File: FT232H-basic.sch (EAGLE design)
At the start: 27 parts, among them IC1 FT232H

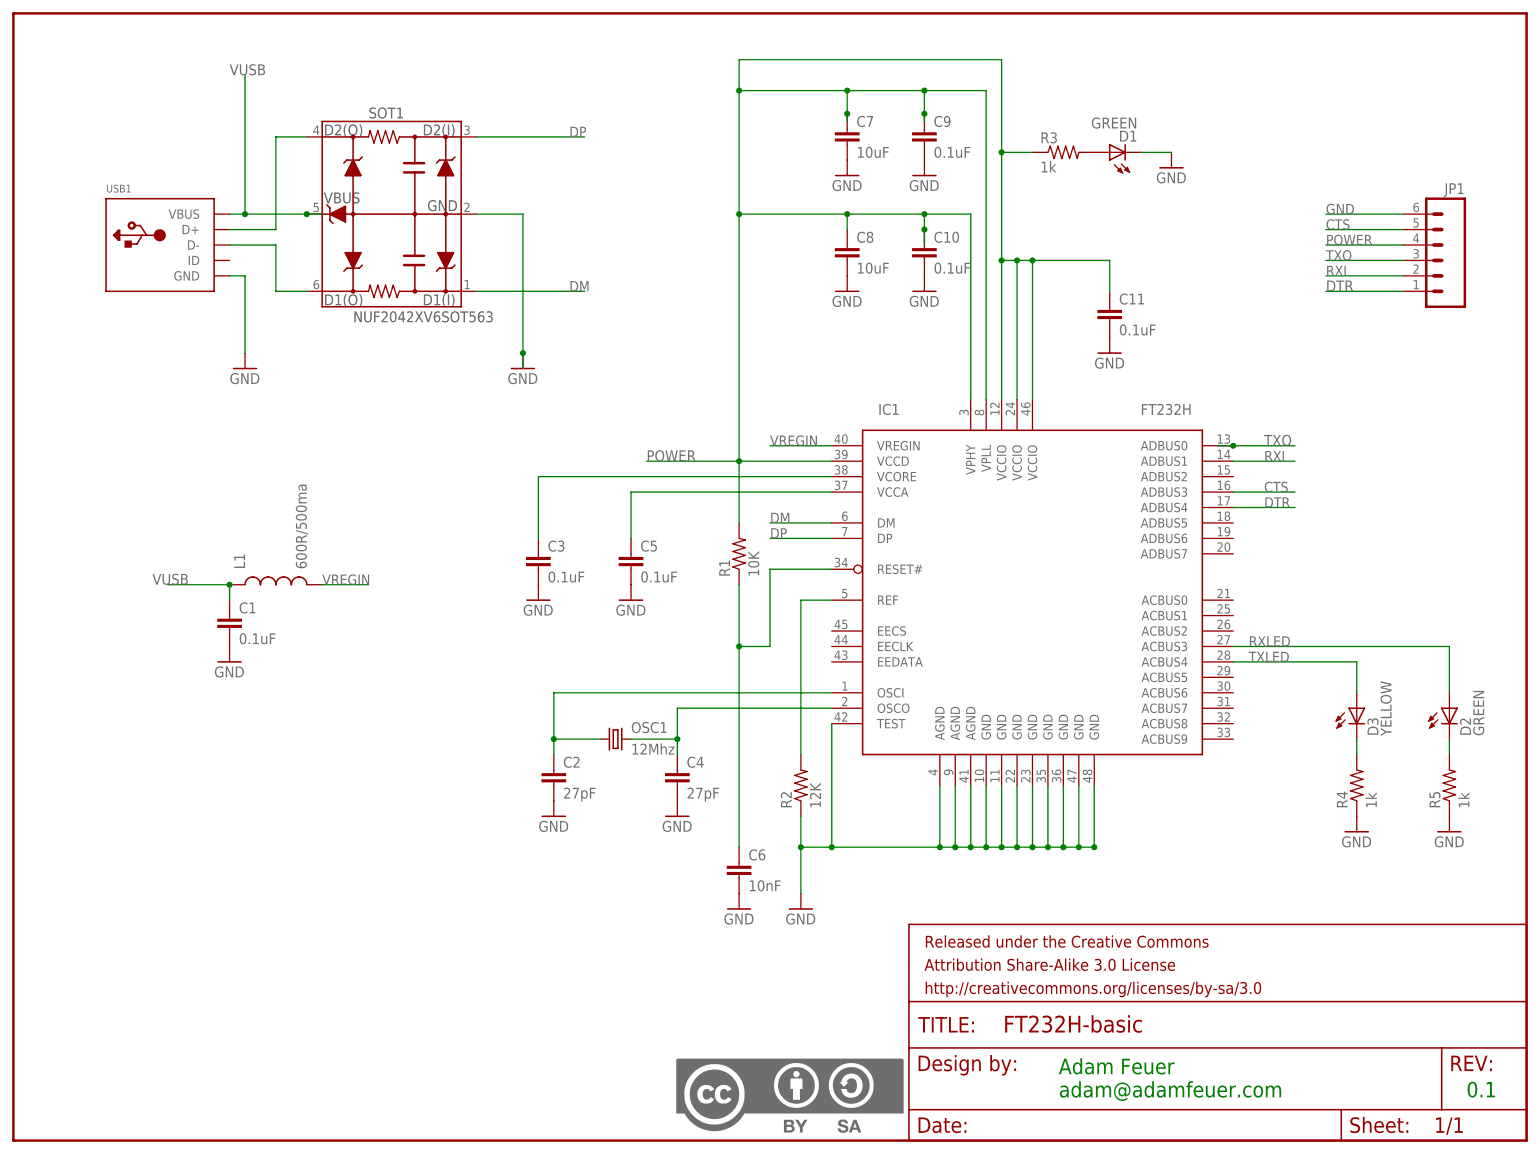
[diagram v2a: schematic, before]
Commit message: minor changes - removed CC logo from schematic (still on board); made layers visible
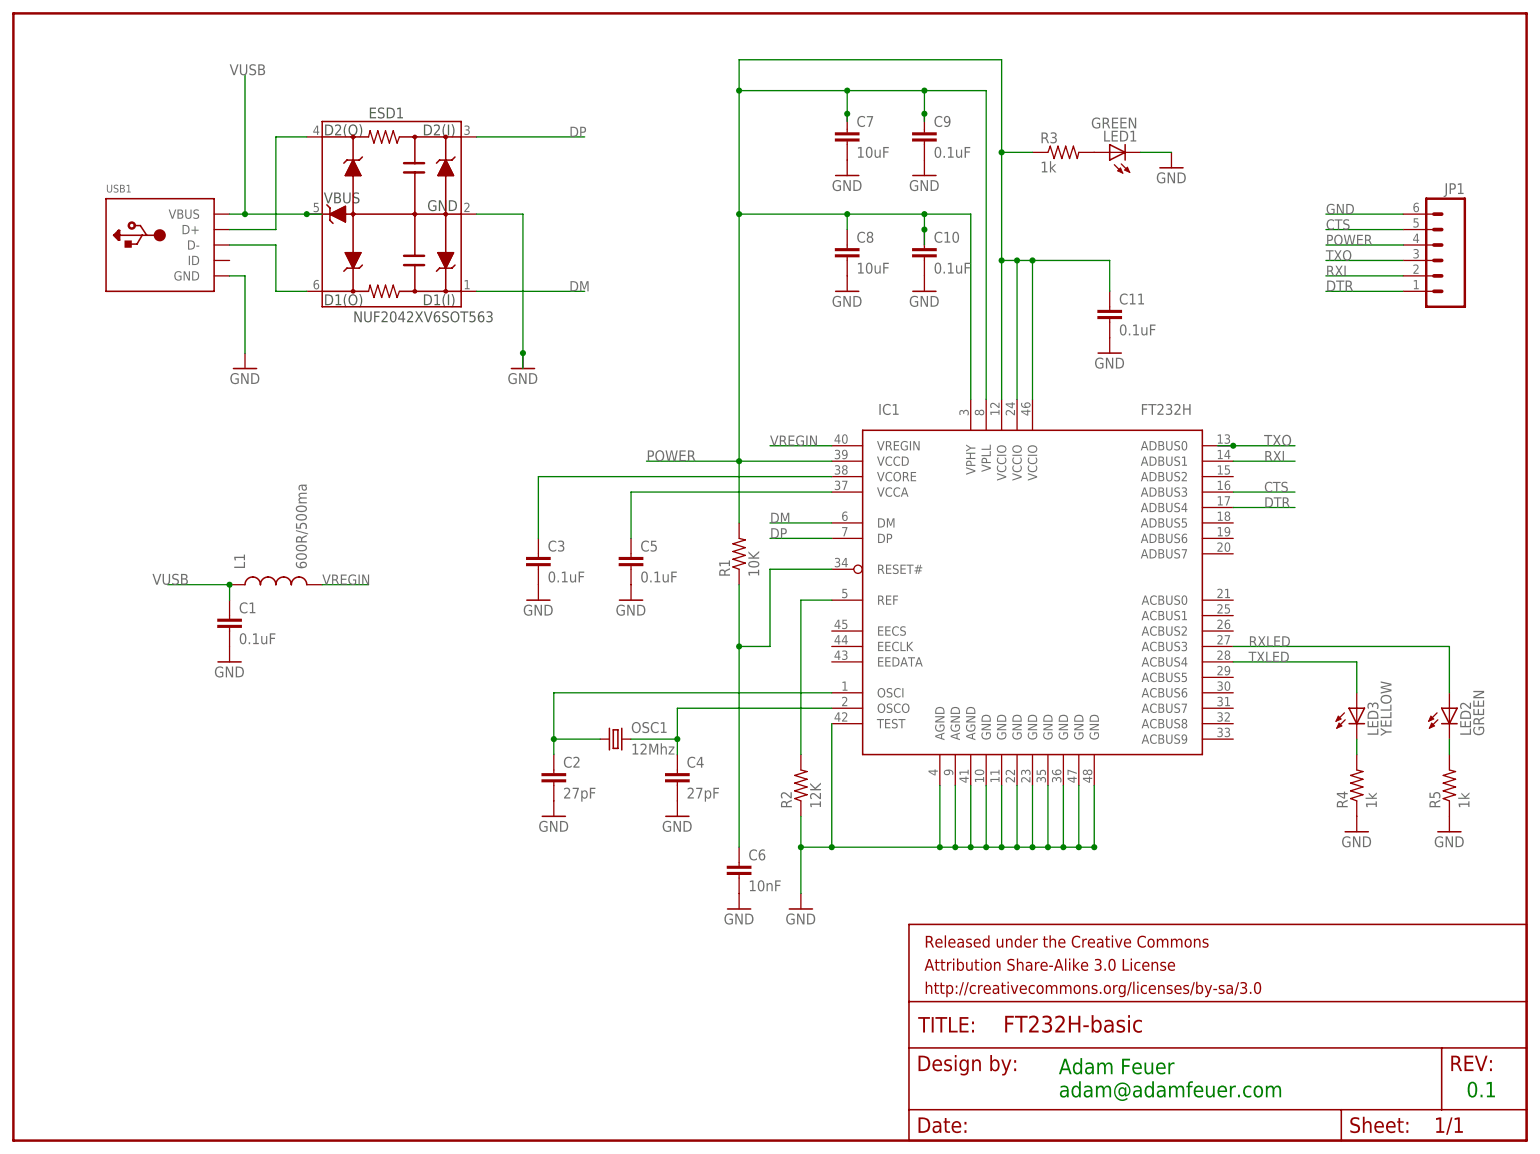
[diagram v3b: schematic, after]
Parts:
- removed U$2: CC-BY-SA, creative-commons:CC-BY-SA
- renumbered D1 to LED1, D2 to LED2, D3 to LED3, SOT1 to ESD1
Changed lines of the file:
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@@
 <part name="GND13" library="SparkFun-Aesthetics" deviceset="GND" device=""/>
 <part name="L1" library="SparkFun-Passives" deviceset="INDUCTOR" device="0603" value="600R/500ma"/>
-<part name="SOT1" library="USB-ESD-protection" deviceset="NUF2042XV6" device="SOT563"/>
+<part name="ESD1" library="USB-ESD-protection" deviceset="NUF2042XV6" device="SOT563"/>
 <part name="USB1" library="USB-Mini-Molex" deviceset="USB-MINIB" device="TH-SLOT"/>
 <part name="GND14" library="SparkFun-Aesthetics" deviceset="GND" device=""/>
 <part name="GND15" library="SparkFun-Aesthetics" deviceset="GND" device=""/>
 <part name="JP1" library="SparkFun-Connectors" deviceset="M06" device="SMD-FEMALE-V2"/>
-<part name="D2" library="SparkFun-LED" deviceset="LED-GREEN" device="0603" value="GREEN"/>
-<part name="D3" library="SparkFun-LED" deviceset="LED-YELLOW" device="0603" value="YELLOW"/>
+<part name="LED2" library="SparkFun-LED" deviceset="LED-GREEN" device="0603" value="GREEN"/>
+<part name="LED3" library="SparkFun-LED" deviceset="LED-YELLOW" device="0603" value="YELLOW"/>
 <part name="R4" library="SparkFun-Resistors" deviceset="1K-1%" device="" value="1k"/>
 <part name="R5" library="SparkFun-Resistors" deviceset="1K-1%" device="" value="1k"/>
 <part name="GND16" library="SparkFun-Aesthetics" deviceset="GND" device=""/>
 <part name="GND17" library="SparkFun-Aesthetics" deviceset="GND" device=""/>
-<part name="D1" library="SparkFun-LED" deviceset="LED-GREEN" device="0603" value="GREEN"/>
+<part name="LED1" library="SparkFun-LED" deviceset="LED-GREEN" device="0603" value="GREEN"/>
 <part name="OSC1" library="SparkFun-FreqCtrl" deviceset="CRYSTAL" device="5X3" value="12Mhz"/>
 <part name="FRAME1" library="SparkFun-Aesthetics" deviceset="FRAME-LETTER" device=""/>
-<part name="U$2" library="creative-commons" deviceset="CC-BY-SA" device=""/>
 </parts>
 <sheets>
@@
 <instance part="GND13" gate="1" x="35.56" y="78.74"/>
 <instance part="L1" gate="G$1" x="43.18" y="91.44" rot="R90"/>
-<instance part="SOT1" gate="G$1" x="63.5" y="152.4"/>
+<instance part="ESD1" gate="G$1" x="63.5" y="152.4"/>
 <instance part="USB1" gate="G$1" x="25.4" y="147.32"/>
 <instance part="GND14" gate="1" x="38.1" y="127"/>
 <instance part="GND15" gate="1" x="83.82" y="127"/>
 <instance part="JP1" gate="G$1" x="233.68" y="144.78" rot="MR0"/>
-<instance part="D2" gate="G$1" x="236.22" y="71.12"/>
-<instance part="D3" gate="G$1" x="220.98" y="71.12"/>
+<instance part="LED2" gate="G$1" x="236.22" y="71.12"/>
+<instance part="LED3" gate="G$1" x="220.98" y="71.12"/>
 <instance part="R4" gate="G$1" x="220.98" y="58.42" rot="R90"/>
 <instance part="R5" gate="G$1" x="236.22" y="58.42" rot="R90"/>
 <instance part="GND16" gate="1" x="220.98" y="50.8"/>
 <instance part="GND17" gate="1" x="236.22" y="50.8"/>
-<instance part="D1" gate="G$1" x="180.34" y="162.56" rot="R90"/>
+<instance part="LED1" gate="G$1" x="180.34" y="162.56" rot="R90"/>
 <instance part="OSC1" gate="G$1" x="99.06" y="66.04"/>
 <instance part="FRAME1" gate="G$1" x="0" y="0"/>
 <instance part="FRAME1" gate="G$2" x="147.32" y="0"/>
-<instance part="U$2" gate="G$1" x="108.712" y="0.508"/>
 </instances>
 <busses>
@@
 <pinref part="GND12" gate="1" pin="GND"/>
 <wire x1="185.42" y1="162.56" x2="190.5" y2="162.56" width="0.1524" layer="91"/>
-<pinref part="D1" gate="G$1" pin="C"/>
+<pinref part="LED1" gate="G$1" pin="C"/>
 </segment>
 <segment>
@@
 </segment>
 <segment>
-<pinref part="SOT1" gate="G$1" pin="GND"/>
+<pinref part="ESD1" gate="G$1" pin="GND"/>
 <wire x1="76.2" y1="152.4" x2="83.82" y2="152.4" width="0.1524" layer="91"/>
 <wire x1="83.82" y1="152.4" x2="83.82" y2="129.54" width="0.1524" layer="91"/>
@@
 <pinref part="USB1" gate="G$1" pin="VBUS"/>
 <wire x1="35.56" y1="152.4" x2="38.1" y2="152.4" width="0.1524" layer="91"/>
-<pinref part="SOT1" gate="G$1" pin="VBUS"/>
+<pinref part="ESD1" gate="G$1" pin="VBUS"/>
 <wire x1="38.1" y1="152.4" x2="48.26" y2="152.4" width="0.1524" layer="91"/>
 <wire x1="48.26" y1="152.4" x2="50.8" y2="152.4" width="0.1524" layer="91"/>
@@
 <wire x1="35.56" y1="149.86" x2="43.18" y2="149.86" width="0.1524" layer="91"/>
 <wire x1="43.18" y1="149.86" x2="43.18" y2="165.1" width="0.1524" layer="91"/>
-<pinref part="SOT1" gate="G$1" pin="D2(O)"/>
+<pinref part="ESD1" gate="G$1" pin="D2(O)"/>
 <wire x1="43.18" y1="165.1" x2="48.26" y2="165.1" width="0.1524" layer="91"/>
 </segment>
@@
 <wire x1="35.56" y1="147.32" x2="43.18" y2="147.32" width="0.1524" layer="91"/>
 <wire x1="43.18" y1="147.32" x2="43.18" y2="139.7" width="0.1524" layer="91"/>
-<pinref part="SOT1" gate="G$1" pin="D1(O)"/>
+<pinref part="ESD1" gate="G$1" pin="D1(O)"/>
 <wire x1="43.18" y1="139.7" x2="48.26" y2="139.7" width="0.1524" layer="91"/>
 </segment>
@@
 <net name="DP" class="0">
 <segment>
-<pinref part="SOT1" gate="G$1" pin="D2(I)"/>
+<pinref part="ESD1" gate="G$1" pin="D2(I)"/>
 <wire x1="76.2" y1="165.1" x2="93.98" y2="165.1" width="0.1524" layer="91"/>
 <label x="91.44" y="165.1" size="1.6764" layer="95"/>
@@
 <net name="DM" class="0">
 <segment>
-<pinref part="SOT1" gate="G$1" pin="D1(I)"/>
+<pinref part="ESD1" gate="G$1" pin="D1(I)"/>
 <wire x1="76.2" y1="139.7" x2="93.98" y2="139.7" width="0.1524" layer="91"/>
 <label x="91.44" y="139.7" size="1.6764" layer="95"/>
@@
 <pinref part="IC1" gate="G$1" pin="ACBUS3"/>
 <label x="203.2" y="81.28" size="1.6764" layer="95"/>
-<pinref part="D2" gate="G$1" pin="A"/>
+<pinref part="LED2" gate="G$1" pin="A"/>
 <wire x1="200.66" y1="81.28" x2="236.22" y2="81.28" width="0.1524" layer="91"/>
 <wire x1="236.22" y1="81.28" x2="236.22" y2="73.66" width="0.1524" layer="91"/>
@@
 <pinref part="IC1" gate="G$1" pin="ACBUS4"/>
 <label x="203.2" y="78.74" size="1.6764" layer="95"/>
-<pinref part="D3" gate="G$1" pin="A"/>
+<pinref part="LED3" gate="G$1" pin="A"/>
 <wire x1="200.66" y1="78.74" x2="220.98" y2="78.74" width="0.1524" layer="91"/>
 <wire x1="220.98" y1="78.74" x2="220.98" y2="73.66" width="0.1524" layer="91"/>
@@
 <net name="N$10" class="0">
 <segment>
-<pinref part="D3" gate="G$1" pin="C"/>
+<pinref part="LED3" gate="G$1" pin="C"/>
 <pinref part="R4" gate="G$1" pin="2"/>
 <wire x1="220.98" y1="66.04" x2="220.98" y2="63.5" width="0.1524" layer="91"/>
@@
 <net name="N$11" class="0">
 <segment>
-<pinref part="D2" gate="G$1" pin="C"/>
+<pinref part="LED2" gate="G$1" pin="C"/>
 <pinref part="R5" gate="G$1" pin="2"/>
 <wire x1="236.22" y1="66.04" x2="236.22" y2="63.5" width="0.1524" layer="91"/>
@@
 <segment>
 <pinref part="R3" gate="G$1" pin="2"/>
-<pinref part="D1" gate="G$1" pin="A"/>
-</segment>
-</net>
+<pinref part="LED1" gate="G$1" pin="A"/>
+</segment>
+</net>

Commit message: changed out ESD IC to USB 2.0 HS - NXP IP4220CZ6 ; added LittelFuse 0603; changed out connector to 1x06 female through hole
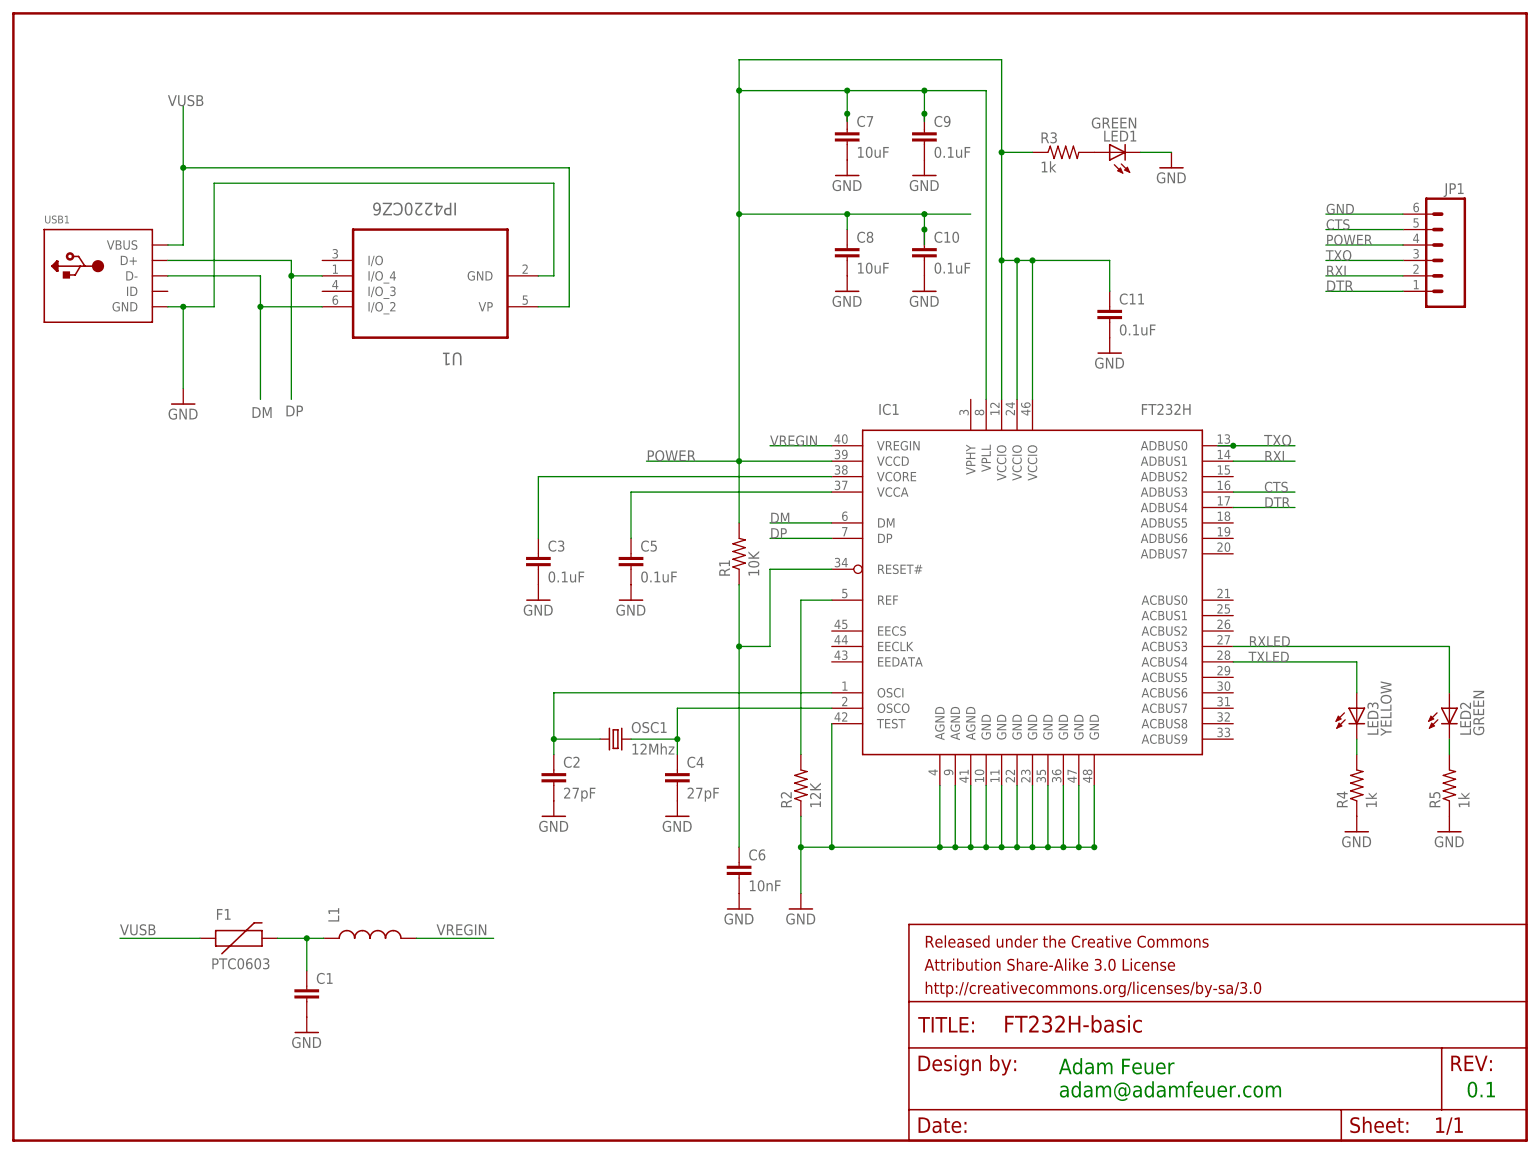
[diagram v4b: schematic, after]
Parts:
- removed ESD1: NUF2042XV6SOT563, USB-ESD-protection:NUF2042XV6SOT563
- added F1: PTC0603, SparkFun-PowerIC:PTC0603
- added U1: IP4220CZ6, NXP_By_element14_Batch_1:IP4220CZ6
- C1: value 0.1uF -> (none); device SparkFun-Capacitors:0.1UF-25V-5%(0603) -> SparkFun-Passives:CAP0603-CAP
- JP1: device SparkFun-Connectors:M06SMD-FEMALE-V2 -> SparkFun-Connectors:M06SIP
- L1: value 600R/500ma -> (none)
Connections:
- removed net N$8: ESD1.D1(O), USB1.D-
- net DM: now also U1.I/O_2, USB1.D-; no longer ESD1.D1(I)
- net DP: now also U1.I/O_4, USB1.D+; no longer ESD1.D2(I)
- net GND: now also U1.GND; no longer ESD1.GND
- net N$6: now also C1.1, F1.2, L1.1; no longer ESD1.D2(O), USB1.D+
- net POWER: no longer IC1.VPHY
- net VUSB: now also F1.1, U1.VP; no longer C1.1, ESD1.VBUS, L1.1
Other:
- moved on the sheet: C1, L1, USB1
